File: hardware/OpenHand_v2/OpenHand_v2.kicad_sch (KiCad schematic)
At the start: 59 parts, among them J1 CONN_MOTOR_1, J10 CONN_FDBK_2, J11 CONN_EMG_2, J12 CONN_SWD, J13 CONN_POS_3, J2 CONN_MOTOR_2, J3 CONN_BATT, J4 CONN_POS_1, J5 CONN_USB_C, J6 CONN_MOTOR_3, J7 CONN_FDBK_1, J8 CONN_EMG_1, J9 CONN_POS_2, SW1 BTN_RST, SW2 SW_Push, U1 STM32F103RETx, Y1 16MHz

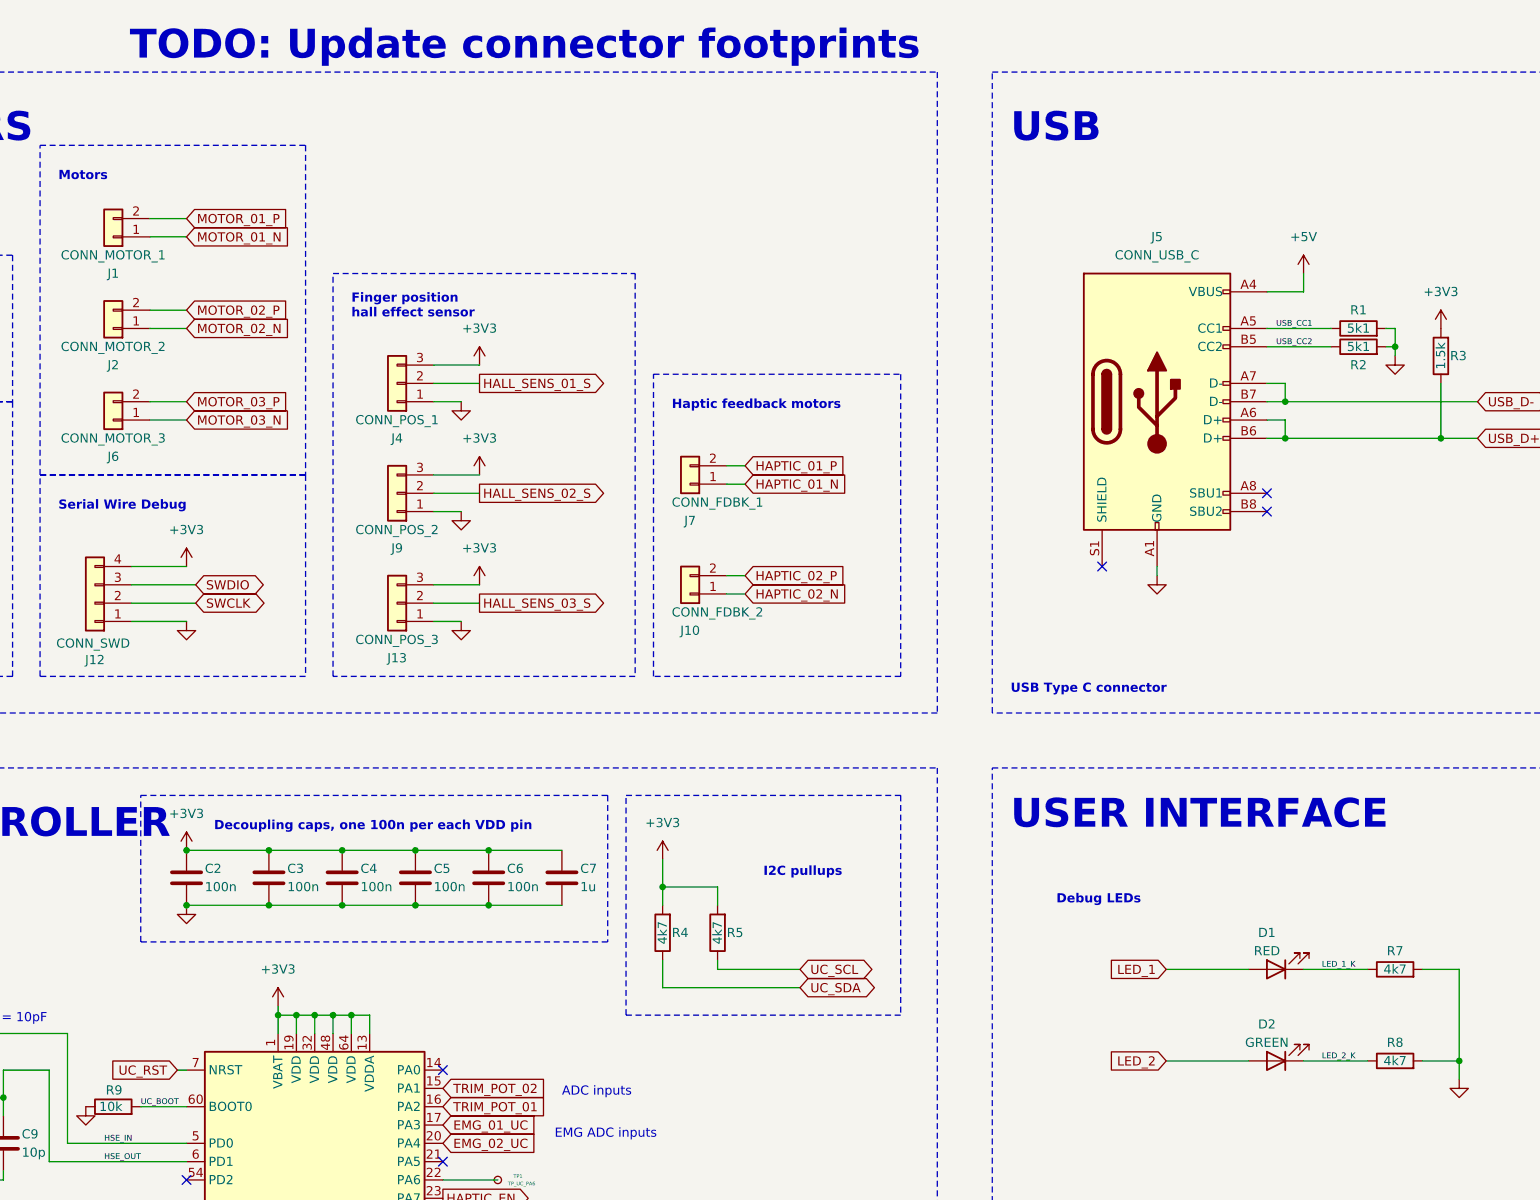
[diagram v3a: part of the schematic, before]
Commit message: EMG sensor quickfix, upadte ADC and DMA config
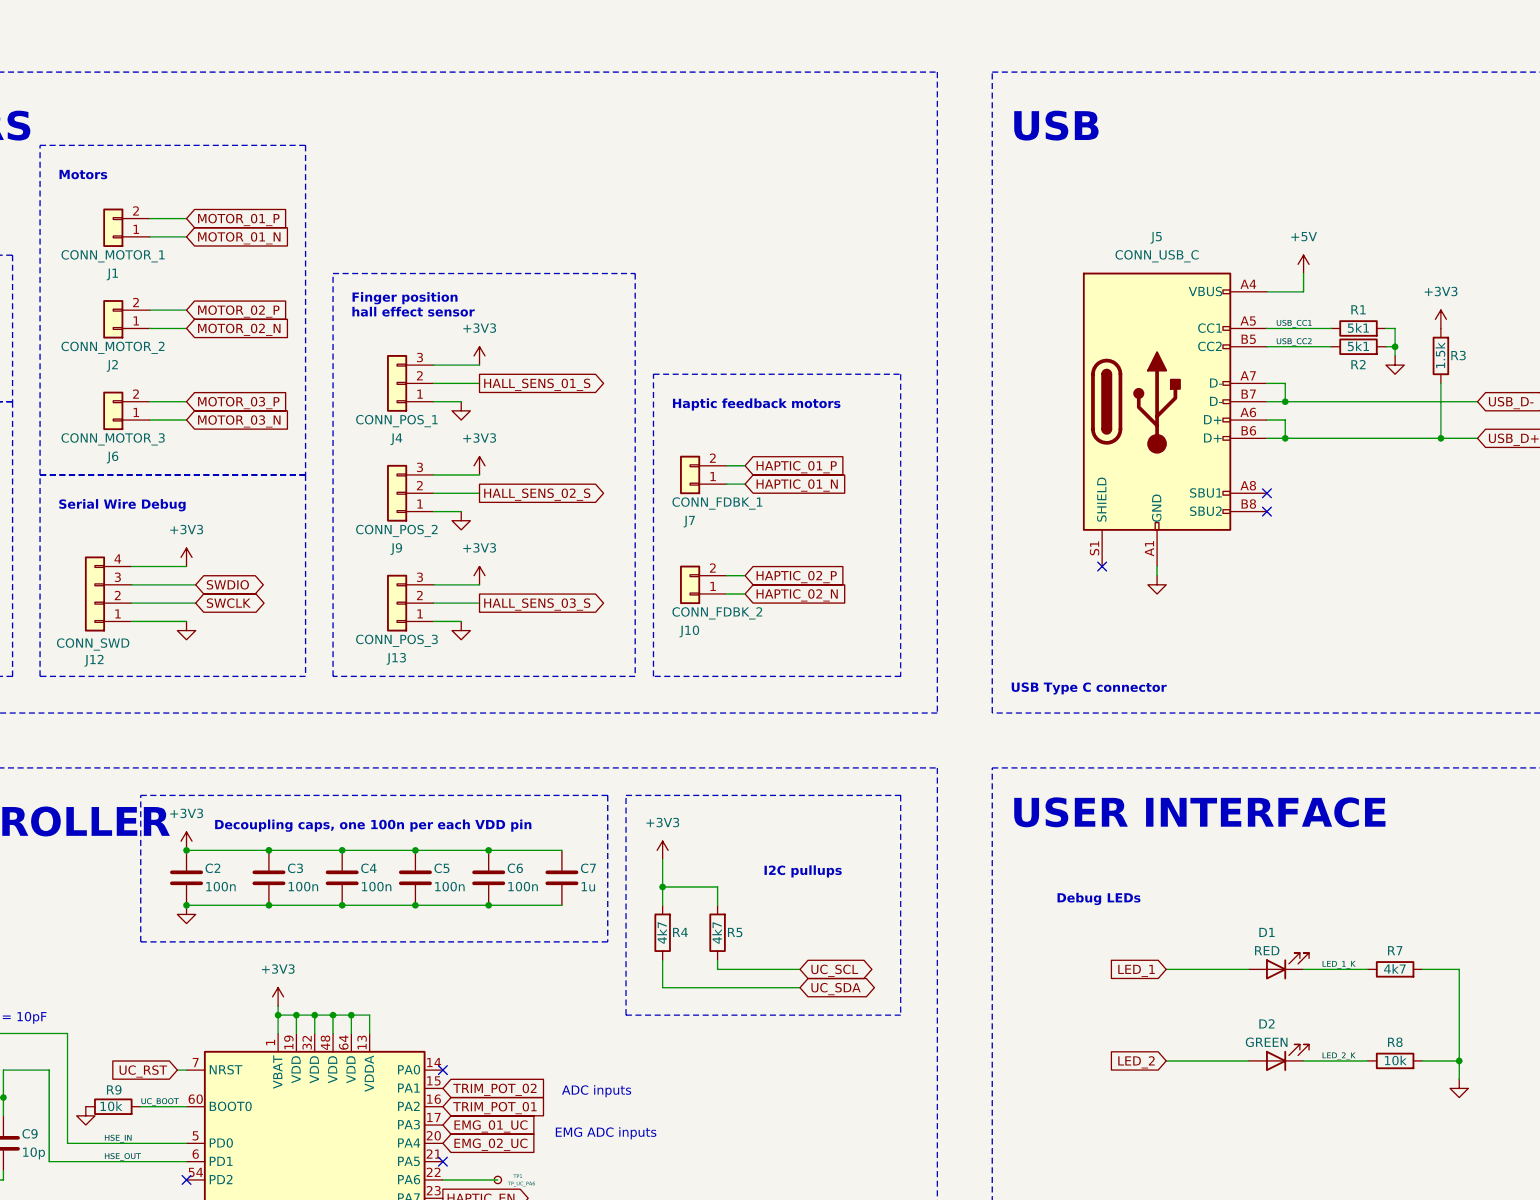
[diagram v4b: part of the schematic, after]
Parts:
- R8: value 4k7 -> 10k
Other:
- note removed: "TODO: Update connector footprints"
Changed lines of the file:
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@@
 		)
 	)
-	(text "TODO: Update connector footprints"
-		(exclude_from_sim no)
-		(at 78.486 19.05 0)
-		(effects
-			(font
-				(size 4 4)
-				(thickness 0.6)
-				(bold yes)
-			)
-			(justify left bottom)
-		)
-	)
 	(text "Just in case I2C"
 		(exclude_from_sim no)
@@
 			)
 		)
-		(property "Value" "4k7"
+		(property "Value" "10k"
 			(at 254 157.48 90)
 			(effects
